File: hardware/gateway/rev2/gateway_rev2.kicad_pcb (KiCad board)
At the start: 2 copper layers, 94 x 78 mm, 68 parts, among them IC1 STM8L151K4T6, IC2 CC1101RGPR, IC5 MB85RC64TAPNF-G-BDERE1, J1 22-28-4044, J2 M20-9770342, U1 IRM-01-3.3, Y1 NX3225GA-26MHZ-TI

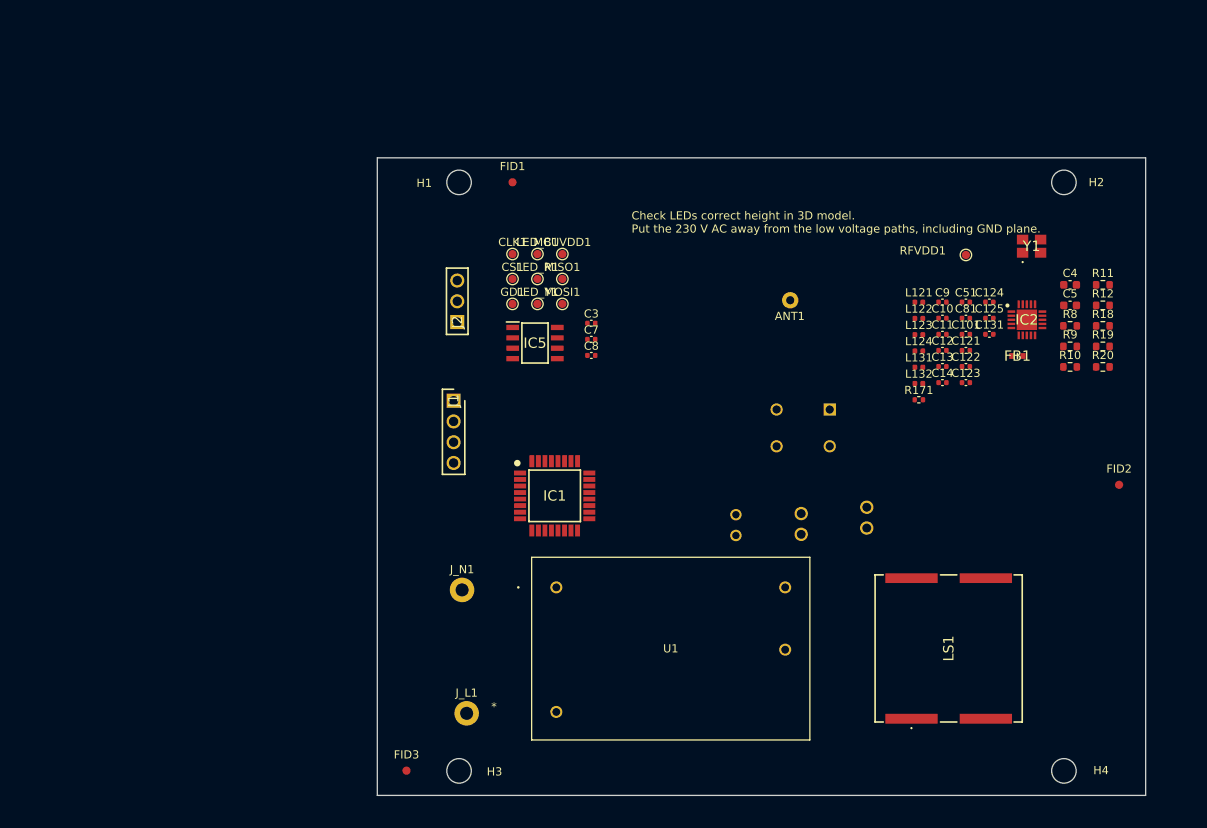
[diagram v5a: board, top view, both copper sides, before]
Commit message: EG-59 Board shape finished. Button, LEDs, AC-DC and buzzer placed.
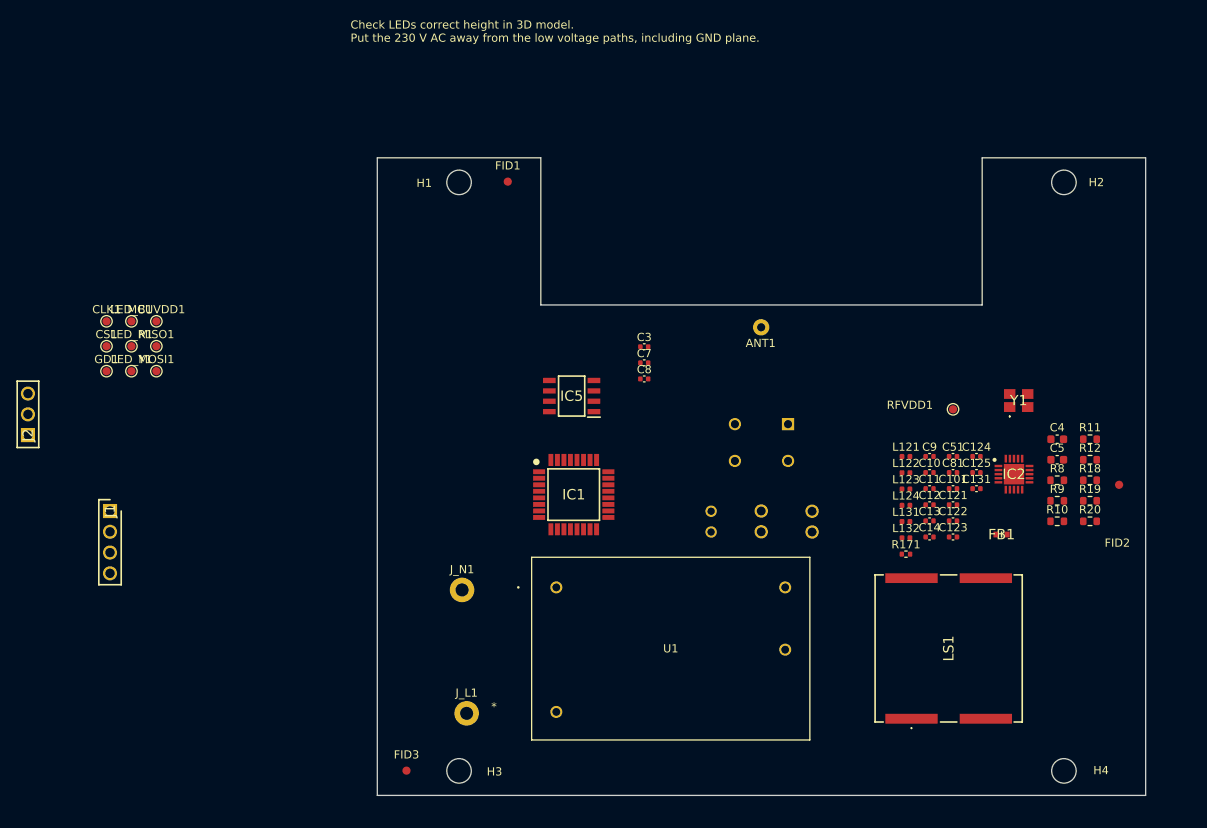
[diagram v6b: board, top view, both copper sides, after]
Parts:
- moved J2 54.3 mm to (137.3, 113.9)
- moved LED_B1 50.3 mm to (149.9, 100.0)
- moved LED_R1 50.3 mm to (149.9, 103.0)
- moved LED_Y1 50.3 mm to (149.9, 106.1)
- moved CLK1 50.3 mm to (146.9, 100.0)
- moved CS1 50.3 mm to (146.9, 103.0)
- moved GD1 50.3 mm to (146.9, 106.1)
- moved MCUVDD1 50.3 mm to (153.0, 100.0)
- moved MISO1 50.3 mm to (153.0, 103.0)
- moved MOSI1 50.3 mm to (153.0, 106.1)
- moved J1 44.1 mm to (147.3, 123.2)
- moved FB1 21.9 mm to (256.4, 126.1)
- moved R171 19.0 mm to (244.7, 128.5)
- moved C122 19.0 mm to (250.4, 124.4)
- moved C123 19.0 mm to (250.4, 126.4)
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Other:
- outline, holes or cut-outs redrawn

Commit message: EG-59 RF components place defined.
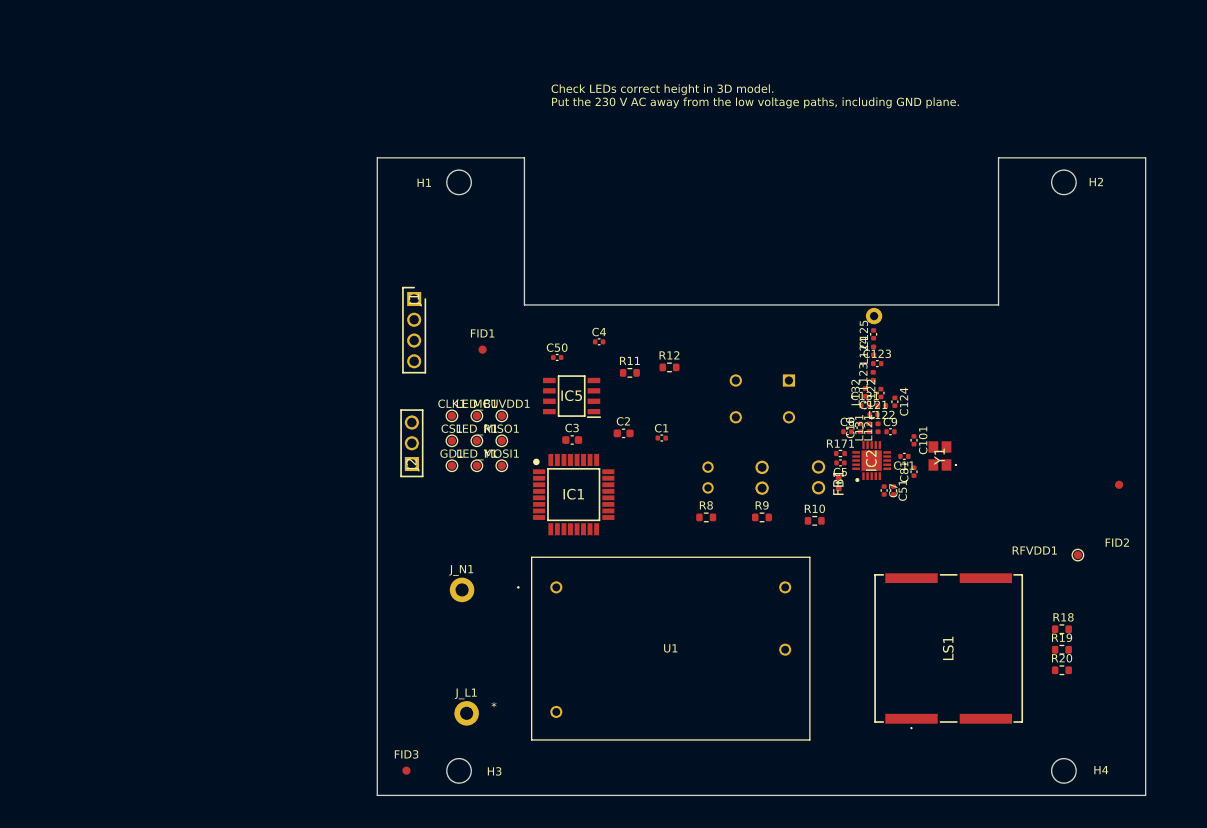
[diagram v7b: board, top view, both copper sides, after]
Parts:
- moved C3 59.4 mm to (203.8, 114.5)
- moved R11 56.9 mm to (210.9, 106.3)
- moved C2 53.0 mm to (210.1, 113.7)
- moved R12 52.7 mm to (215.7, 105.6)
- moved J2 47.1 mm to (184.2, 117.5)
- moved J1 45.4 mm to (184.5, 97.3)
- moved LED_R1 43.8 mm to (192.2, 114.6)
- moved LED_Y1 43.8 mm to (192.2, 117.7)
- moved LED_B1 43.8 mm to (192.2, 111.6)
- moved CS1 43.8 mm to (189.1, 114.6)
- moved GD1 43.8 mm to (189.1, 117.7)
- moved MISO1 43.8 mm to (195.2, 114.6)
- moved MOSI1 43.8 mm to (195.2, 117.7)
- moved CLK1 43.8 mm to (189.1, 111.6)
- moved MCUVDD1 43.8 mm to (195.2, 111.6)
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- renumbered C3 to C1, C13 to C10, C14 to C11, C4 to C2, C5 to C3, C7 to C4, C10 to C5, C8 to C50, C12 to C6, C9 to C7, C11 to C9
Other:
- outline, holes or cut-outs redrawn

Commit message: EG-59 RF Components placed. All passive components 0402.
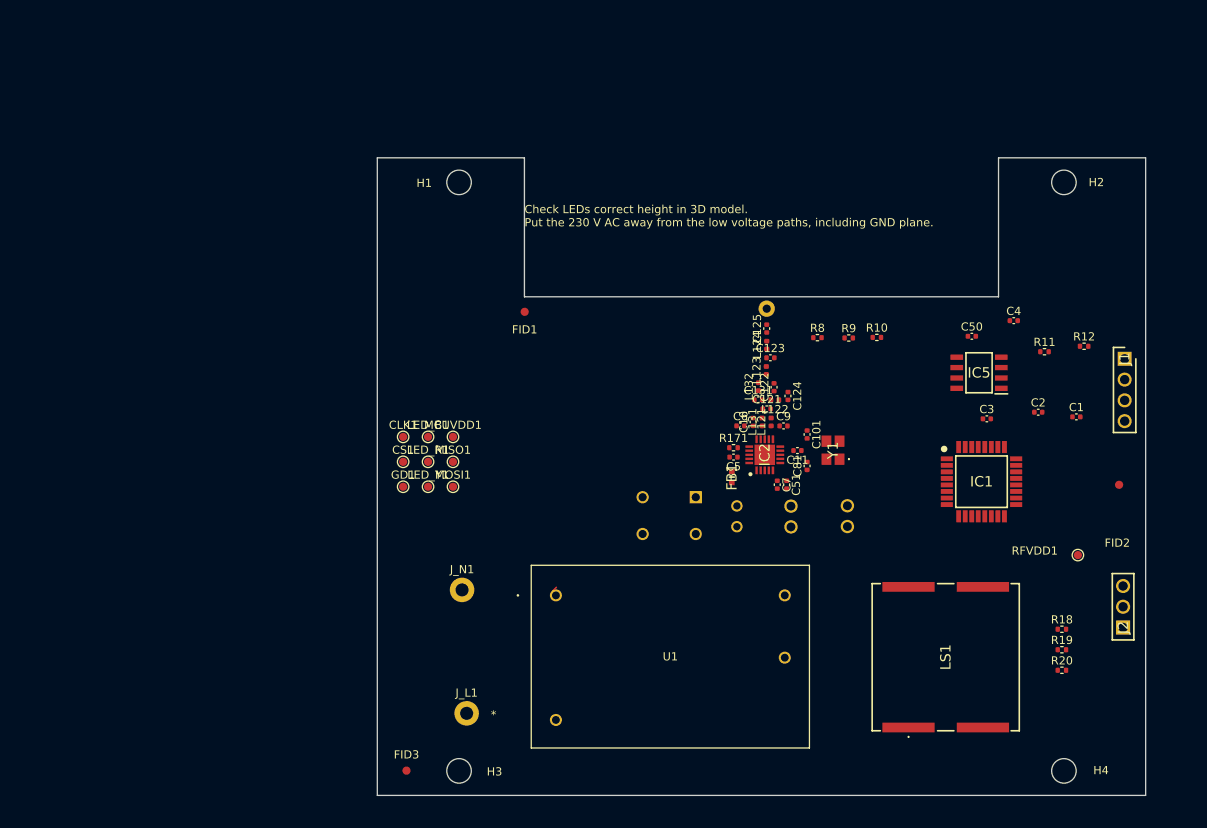
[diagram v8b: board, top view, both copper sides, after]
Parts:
- C2, C3: footprint Capacitor_SMD:C_0603_1608Metric -> Capacitor_SMD:C_0402_1005Metric
- R10, R11, R12, R18, R19, R20, R8, R9: footprint Resistor_SMD:R_0603_1608Metric -> Resistor_SMD:R_0402_1005Metric
- moved J2 89.3 mm to (271.2, 137.5)
- moved J1 87.2 mm to (271.4, 104.6)
- moved C2 50.8 mm to (260.9, 111.1)
- moved C4 50.8 mm to (257.9, 99.9)
- moved C50 50.8 mm to (252.7, 101.8)
- moved R12 50.8 mm to (266.5, 103.0)
- moved C3 50.8 mm to (254.6, 111.9)
- moved R11 50.8 mm to (261.6, 103.7)
- moved C1 50.8 mm to (265.5, 111.7)
- moved IC5 49.9 mm to (253.6, 106.3)
- moved IC1 49.9 mm to (253.9, 119.6)
- moved R8 25.9 mm to (233.8, 102.0)
- moved R9 24.4 mm to (237.7, 102.0)
- moved R10 23.7 mm to (241.1, 102.0)
- moved S1 18.3 mm to (219.0, 121.5)
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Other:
- outline, holes or cut-outs redrawn
